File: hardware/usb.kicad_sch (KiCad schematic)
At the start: 29 parts, among them J3 USB_C_Receptacle, Q1 Q_NMOS_DGS, Q2 MBT2222ADW1T1, U10 CP2102N-Axx-xQFN24, U11 74LVC2G126GT,115, U8 MAX8881EUT33+T, U9 ISL54225

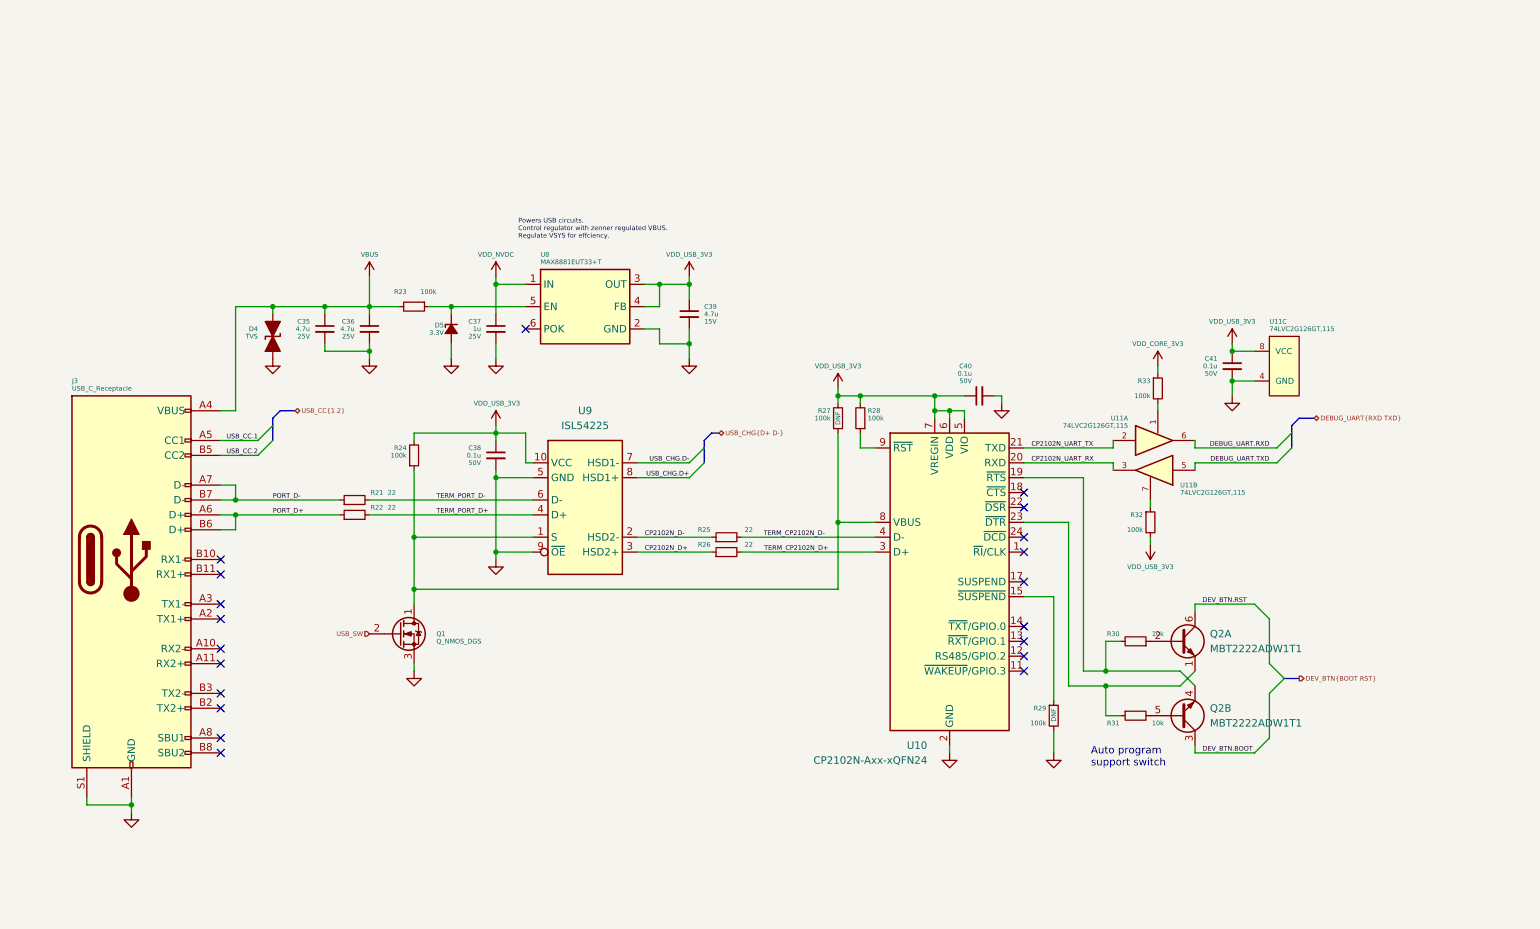
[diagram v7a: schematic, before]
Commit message: initial component placement and design simplification
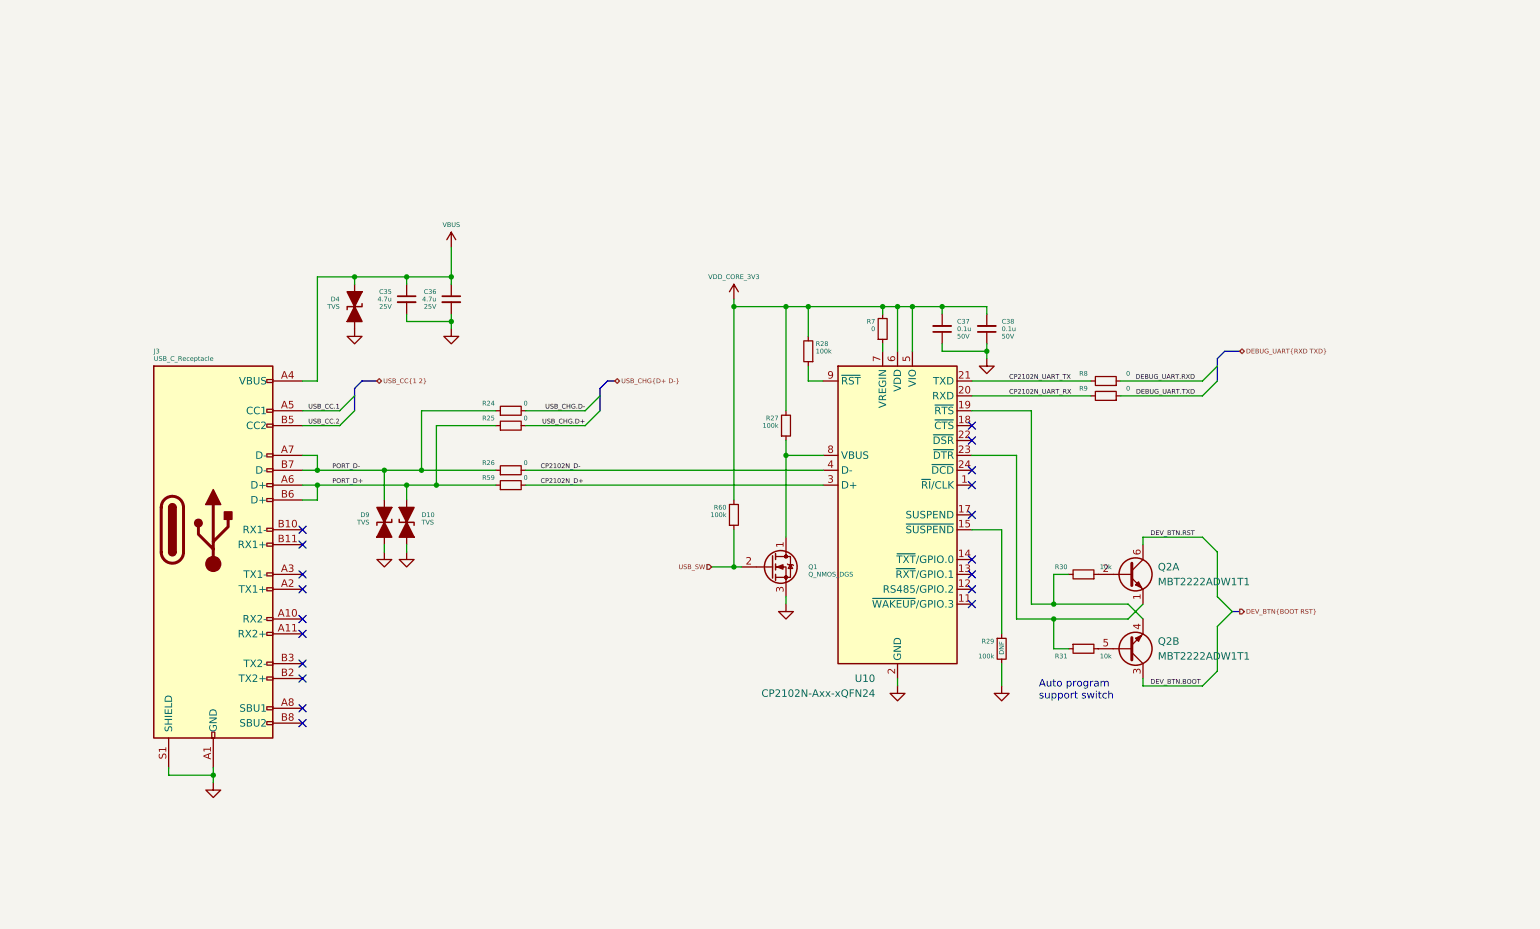
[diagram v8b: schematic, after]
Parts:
- removed C39: 4.7u, Capacitor_SMD:C_0603_1608Metric, symbol Device:C_Small
- removed C40, C41: 0.1u, Capacitor_SMD:C_0402_1005Metric, symbol Device:C_Small
- removed D5: 3.3V, Diode_SMD:D_SOD-523, symbol Device:D_Zener_Small_Filled
- removed R21, R22: 22, Resistor_SMD:R_0402_1005Metric, symbol Device:R_Small
- removed R23, R32, R33: 100k, Resistor_SMD:R_0402_1005Metric, symbol Device:R_Small
- removed U11: 74LVC2G126GT,115, Package_SON:X2SON-8_1.4x1mm_P0.35mm, symbol 74xGxx:74LVC2G125
- removed U8: MAX8881EUT33+T, Package_TO_SOT_SMD:SOT-23-6, symbol bt_PMIC_Linear:MAX8881EUT33+T
- removed U9: ISL54225, Package_DFN_QFN:DFN-10-1EP_3x3mm_P0.5mm_EP1.55x2.48mm, symbol bt_IF_USB:ISL54225
- added D10, D9: TVS, Diode_SMD:D_SOD-523, symbol Device:D_TVS_Filled
- added R59, R7, R8, R9: 0, Resistor_SMD:R_0402_1005Metric, symbol Device:R_Small
- added R60: 100k, Resistor_SMD:R_0402_1005Metric, symbol Device:R_Small
- C37: value 1u -> 0.1u; footprint Capacitor_SMD:C_0603_1608Metric -> Capacitor_SMD:C_0402_1005Metric; Voltage 25V -> 50V
- R24: value 100k -> 0
- R25, R26: value 22 -> 0
- R27: DNF DNF -> (none)
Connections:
- net VDD_NVDC is gone; now on net GND: C37.1
- net 3V3_CORE: now also C37.2, C38.2, R27.2, R28.2, U10.5 (VIO), U10.6 (VDD), R60.2, R7.2
- net CP2102N_D+: now also U10.3 (D+), R59.2; no longer R26.1
- net CP2102N_D-: now also R26.2, U10.4 (D-); no longer R25.1
- net CP2102N_UART_RX: now also R9.2
- net CP2102N_UART_TX: now also R8.2
- net DEBUG_UART.RXD: now also R8.1
- net DEBUG_UART.TXD: now also R9.1
- net GND: now also C38.1, D10.1 (A1), D9.1 (A1); no longer C37.2, C38.2
- net PORT_D+: now also R25.1, D10.2 (A2), R59.1
- net PORT_D-: now also R24.1, R26.1, D9.2 (A2)
- net USB_CHG.D+: now also R25.2
- net USB_CHG.D-: now also R24.2
- net USB_SW: now also R60.1
- net at Q1.1 (D), R27.1, U10.8 (VBUS): no longer R24.1
- removed net TERM_CP2102N_D+: R26.2, U10.3 (D+)
- removed net TERM_CP2102N_D-: R25.2, U10.4 (D-)
- removed net VDD_USB_3V3: C38.1, R24.2, R27.2, R28.2, U10.5 (VIO), U10.6 (VDD), U10.7 (VREGIN)
- new net: R7.1, U10.7 (VREGIN)
- no-connect marks 20 -> 19
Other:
- note removed: "Powers USB circuits. Control regulator with zenner regulated VBUS. Regulate VSYS for effciency."
- moved on the sheet: C35, C36, D4, J3, Q1, Q2A, Q2B, R27, R28, R29, R30, R31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
